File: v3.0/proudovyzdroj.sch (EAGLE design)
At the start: 27 parts, among them IC1 LM358N, Q1 IRF512

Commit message: základní schéma
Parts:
- added C6: (no value), rcl:CPOL-EUE3.5-8
- added D3: (no value), diode:SCHOTTKY-DIODESMC
- added R11, R12: (no value), rcl:R-EU_R0805
- added T1: (no value), transistor:BC337-40-NPN-TO92-CBE
- added T2: (no value), transistor-neu-to92:-PNP-TO220V
- added U$5, U$6: MCP4726, DAC:MCP4726
- added ZD2: (no value), devices:DIODE_ZENER5
- D2: value 1N4004 -> (none); device diode:1N4004 -> diode:SCHOTTKY-DIODESMC
- IC2: value (none) -> LM358N; device v-reg:LM317TS -> linear:LM358N
- R5: device rcl:POTENTIOMETER_PT-10S -> rcl:R-EU_R0805
- R6: device rcl:POTENTIOMETER_PT-10S -> rcl:R-TRIMM3339P
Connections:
- removed net A0: R10.2, R9.A, R9.S
- new net N$13: C1.+, D1.A, R6.E, R9.E, T2.C, X1-2.KL
- new net N$14: R12.1, T2.B
- new net N$15: C3.+, C4.+, C5.+, D1.C, R4.2, T2.E, U$2.2, U$4.2
- new net N$16: R12.2, R4.1, T1.C
- new net N$4: R11.1, T1.B
- new net SCL: U$5.SCL, U$6.SCL
- new net SDA: U$5.SDA, U$6.SDA
- net A1: now also IC2A.OUT, R7.2, ZD2.C; no longer IC1B.OUT
- net GND: now also C4.-, C5.-, C6.-, D2.A, D3.A, IC2P.V-, T1.E, U$1.GND, U$1.SD, U$3.GND, U$3.SD, U$5.VSS, U$6.VSS, ZD2.A; no longer R6.1
- net N$1: now also IC2A.+IN; no longer IC1B.+IN
- net N$10: now also D3.C
- net N$11: now also IC1B.-IN, R6.A, R6.S; no longer C2.+, D2.A, IC2.ADJ, R4.1, R5.3
- net N$12: now also IC1B.OUT, R11.2; no longer R6.2, R7.1
- net N$3: now also IC2A.-IN; no longer IC1B.-IN
- net N$5: now also R10.2, R7.1, R9.A, R9.S; no longer C1.+, D1.A, D2.C, IC2.OUT, R4.2, R9.E, X1-2.KL
- net N$6: now also U$5.OUT; no longer R6.3
- net N$8: now also D2.C
- net N$9: now also IC1B.+IN, U$6.OUT; no longer C3.+, D1.C, IC2.IN, U$2.2, U$4.2
- net VCC: now also U$5.VDD, U$5.VREF, U$6.VDD, U$6.VREF; no longer R7.2
- net VCC/2: now also C2.+, C6.+, IC2P.V+
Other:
- moved on the sheet: ARDUINO_NANO1, C1, C2, C3, C4, C5, D1, IC1B, R4, R7, U$2, U$4

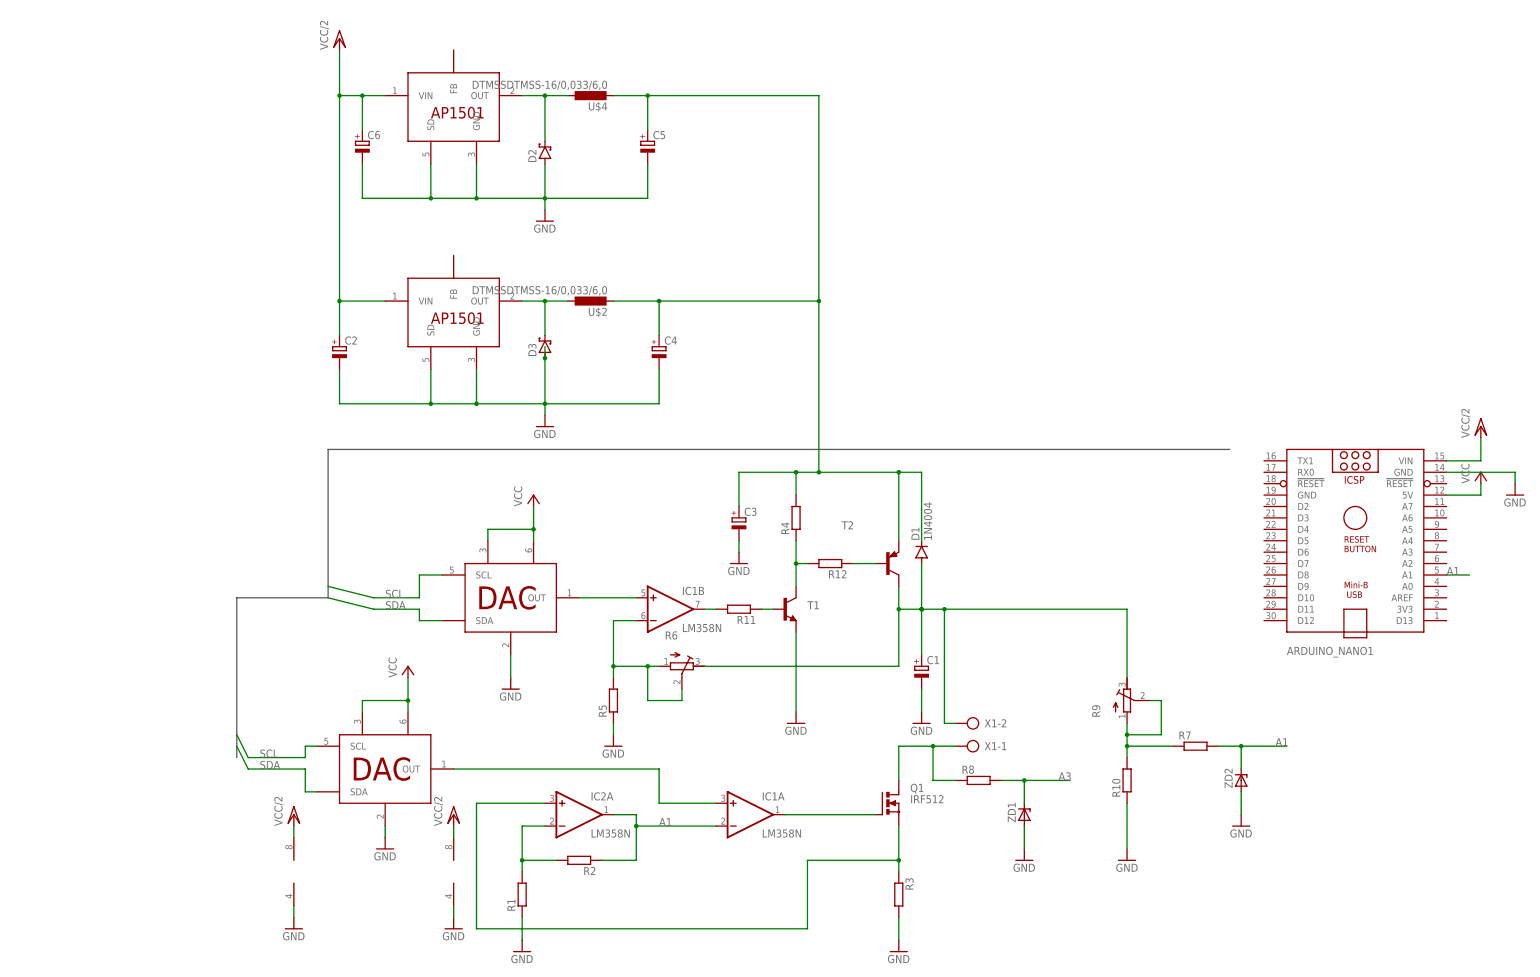
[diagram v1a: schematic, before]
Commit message: náznak řízení spínané části, úklid schématu
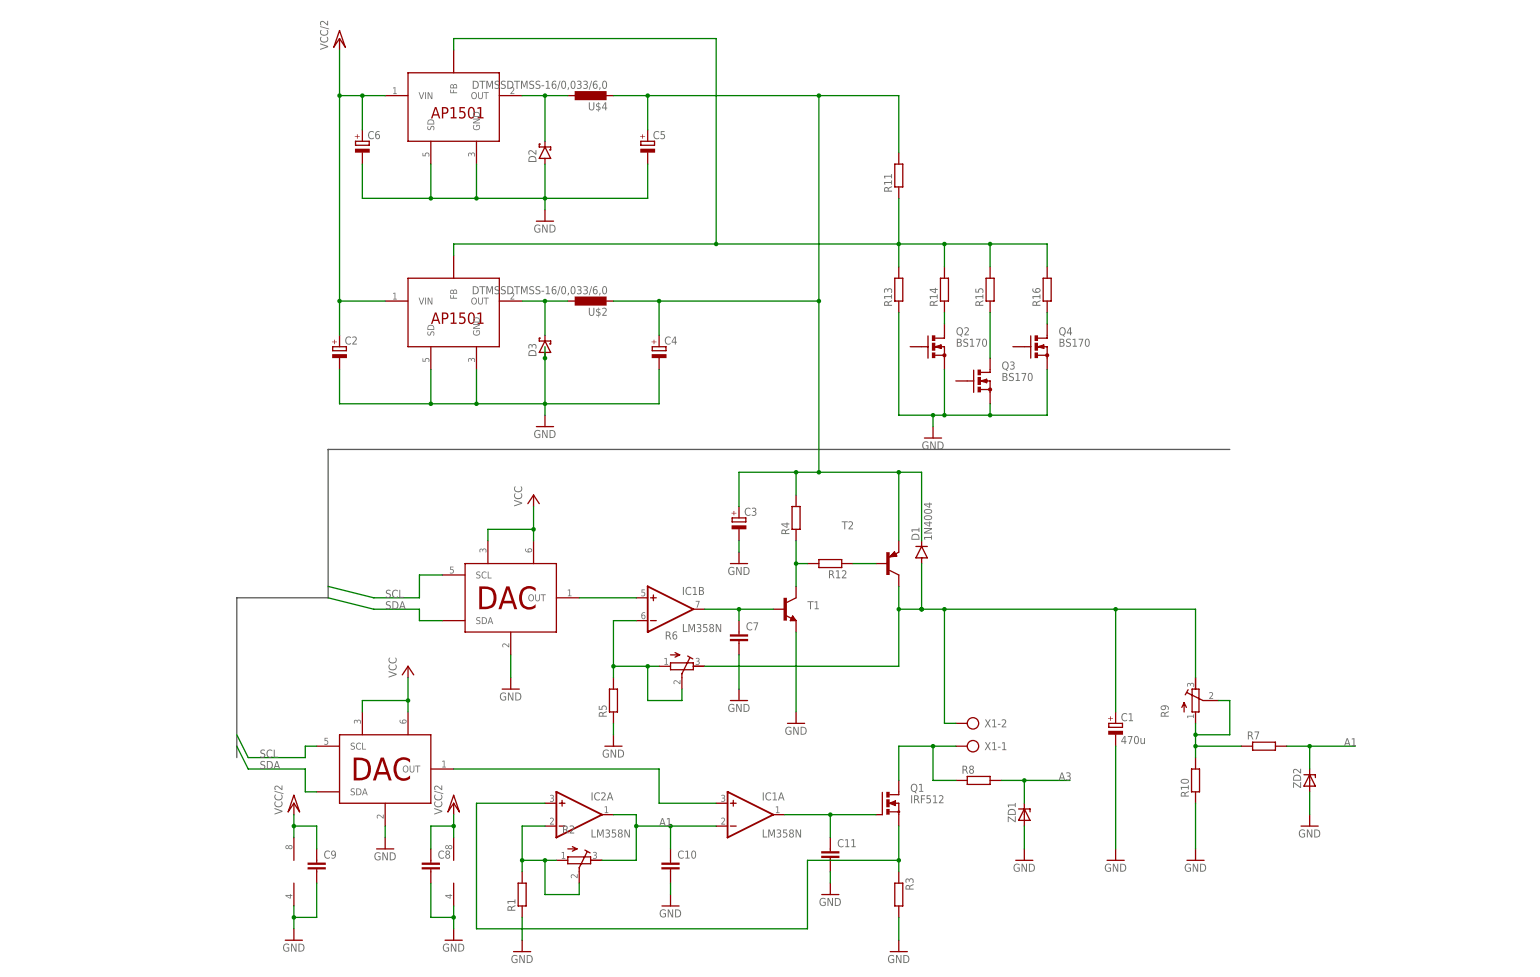
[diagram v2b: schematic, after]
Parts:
- removed ARDUINO_NANO1: (no value), ArduinoNanoV30:ARDUINO_NANO
- added C10, C11, C7, C8, C9: (no value), rcl:C-EUC0805
- added Q2, Q3, Q4: BS170, transistor-small-signal:BS170
- added R13, R14, R15, R16: (no value), rcl_my:R-EU_M0805
- C1: value (none) -> 470u
- R1: device rcl:R-EU_0207/10 -> rcl_my:R-EU_M0805
- R11: device rcl:R-EU_R0805 -> rcl_my:R-EU_M0805
- R2: device rcl:R-EU_0207/10 -> rcl:R-TRIMM3339P
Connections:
- new net N$18: Q3.D, R15.1
- new net N$19: Q4.D, R16.1
- new net N$20: Q2.D, R14.1
- net A1: now also C10.1, R2.E; no longer ARDUINO_NANO1.A1, R2.1
- net GND: now also C10.2, C11.2, C7.2, C8.2, C9.2, Q2.S, Q3.S, Q4.S, R13.1; no longer ARDUINO_NANO1.GND@2
- net N$12: now also C7.1, T1.B; no longer R11.2
- net N$15: now also R11.2
- net N$2: now also C11.1
- net N$3: now also R2.A, R2.S; no longer R2.2
- net N$4: now also R13.2, R14.2, R15.2, R16.2, U$1.FB, U$3.FB; no longer T1.B
- net VCC: no longer ARDUINO_NANO1.5V
- net VCC/2: now also C8.1, C9.1; no longer ARDUINO_NANO1.VIN
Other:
- moved on the sheet: C1, R10, R11, R7, R9, ZD2

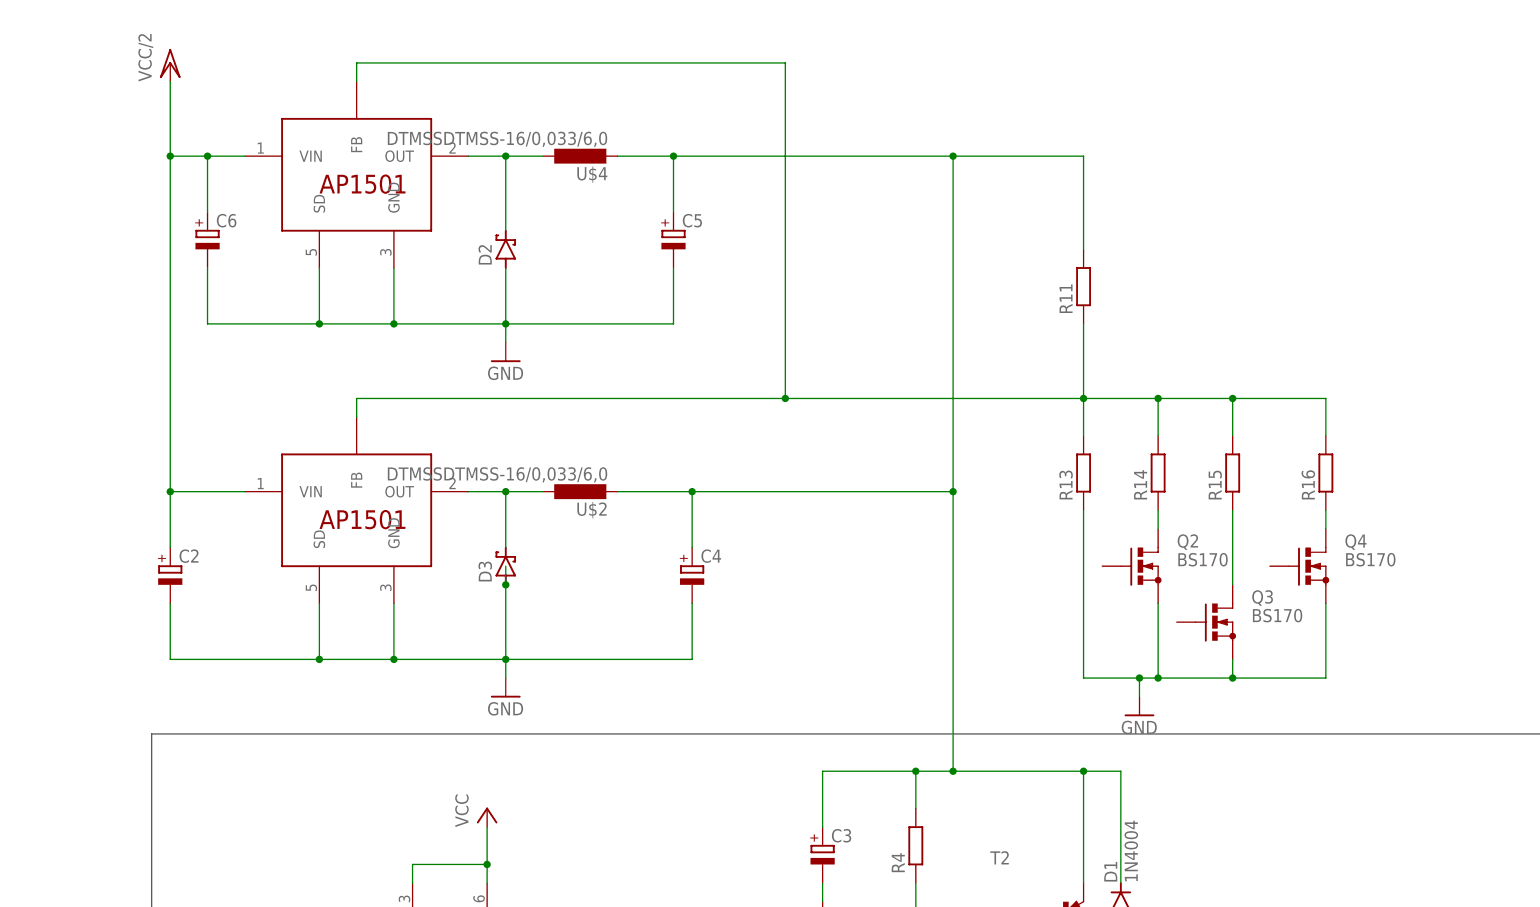
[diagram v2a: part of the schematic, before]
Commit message: přidání řízení DAC1 a ADC
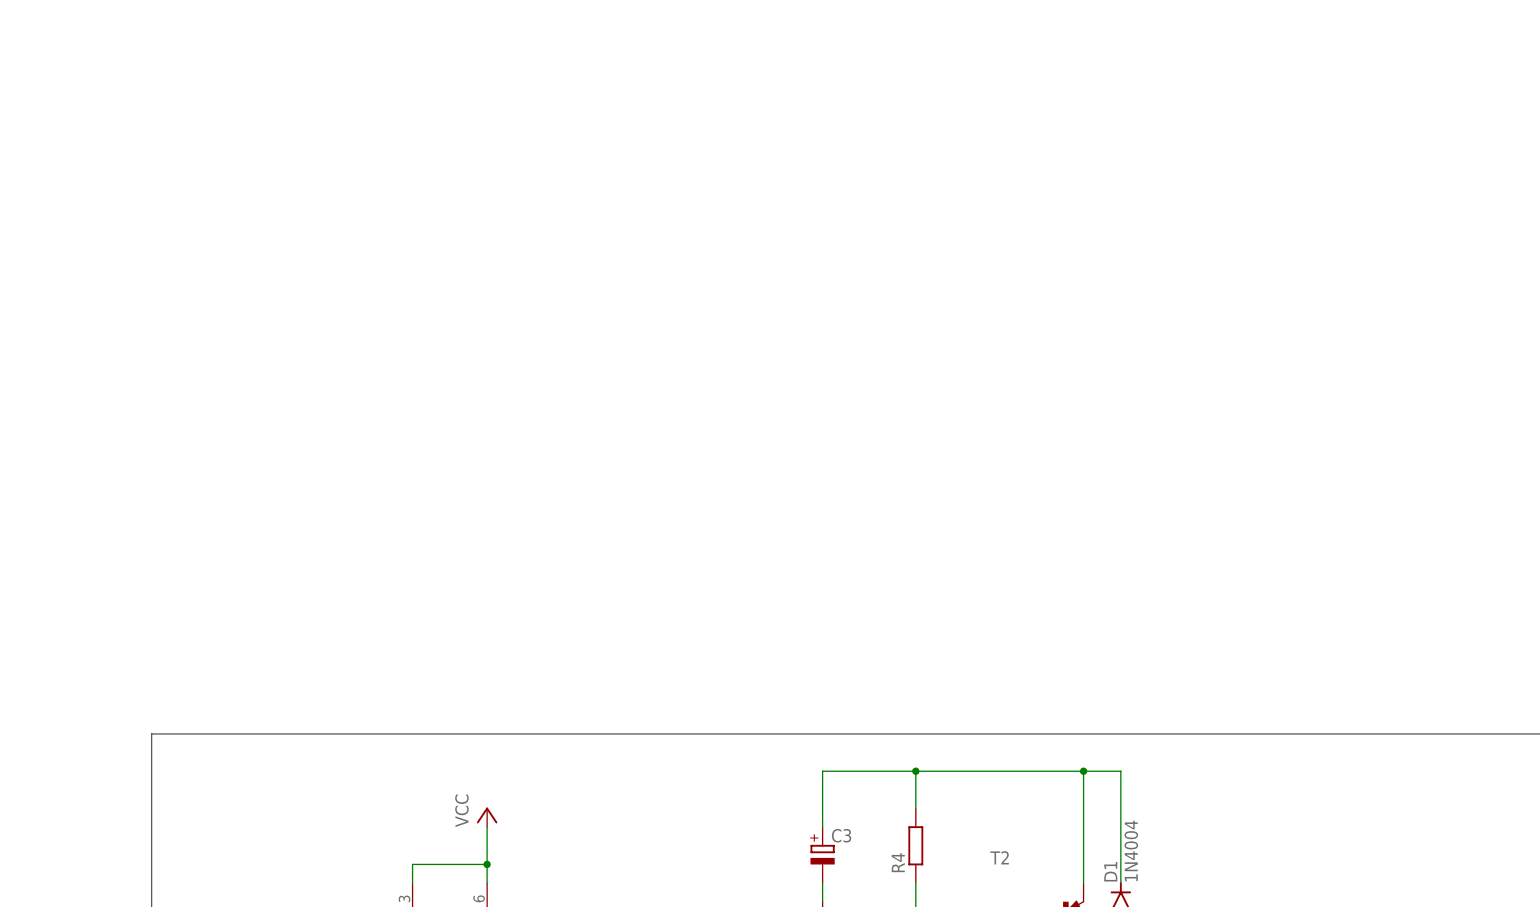
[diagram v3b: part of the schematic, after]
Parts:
- removed C2, C4, C5, C6: (no value), rcl:CPOL-EUE3.5-8
- removed D2, D3: (no value), diode:SCHOTTKY-DIODESMC
- removed Q2, Q3, Q4: BS170, transistor-small-signal:BS170
- removed R11, R13, R14, R15, R16: (no value), rcl_my:R-EU_M0805
- removed U$1, U$3: AP1501TO220, regulators:AP1501TO220
- removed U$2, U$4: DTMSSDTMSS-16/0,033/6,0, induktory a trafa:DTMSSDTMSS-16/0,033/6,0
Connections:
- removed net N$10: D3.C, U$1.OUT, U$2.1
- removed net N$15: C3.+, C4.+, C5.+, D1.C, R11.2, R4.2, T2.E, U$2.2, U$4.2
- removed net N$18: Q3.D, R15.1
- removed net N$19: Q4.D, R16.1
- removed net N$20: Q2.D, R14.1
- removed net N$4: R11.1, R13.2, R14.2, R15.2, R16.2, U$1.FB, U$3.FB
- removed net N$8: D2.C, U$3.OUT, U$4.1
- new net N$24: C3.+, D1.C, R4.2, T2.E
- net GND: no longer C2.-, C4.-, C5.-, C6.-, D2.A, D3.A, Q2.S, Q3.S, Q4.S, R13.1, U$1.GND, U$1.SD, U$3.GND, U$3.SD
- net VCC/2: no longer C2.+, C6.+, U$1.VIN, U$3.VIN

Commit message: přenesení do fusionu
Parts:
- removed R4, R8: (no value), rcl:R-EU_R0805
- removed ZD1: (no value), devices:DIODE_ZENER5
- R5: value (none) -> 1K
- R6: value (none) -> 7K(10K)
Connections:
- removed net N$14: R12.1, T2.B
- removed net N$16: R12.2, R4.1, T1.C
- new net N$4: R12.1, T1.B
- new net N$8: T1.C, T2.B
- net A1: no longer R7.2, ZD2.C
- net A3: now also R7.2, ZD2.C; no longer R8.2, ZD1.C
- net GND: no longer ZD1.A
- net N$12: now also R12.2; no longer T1.B
- net N$13: no longer R9.E
- net N$24: no longer R4.2
- net N$7: now also R9.E; no longer R8.1
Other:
- note added: "3,3V"
- moved on the sheet: R10, R12, R7, R9, T1, ZD2
